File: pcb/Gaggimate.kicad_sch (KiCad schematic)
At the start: 71 parts, among them J1 USB_C_Receptacle, J2 Conn_01x02, J3 Conn_01x03, J4 Conn_01x04, J5 Conn_01x04, J6 Conn_01x10, J7 Conn_01x02, K1 Relay_SPDT, K2 Relay_SPDT, K3 Relay_SPDT, Q1 MMBT3904, Q2 MMBT3904, Q3 MMBT3904, SW1 SW_Push, SW2 SW_Push, U1 ESP32-S3-WROOM-1, U2 AMS1117-3.3, U3 LTV-817S, U4 LTV-817S, U5 LTV-817S, U6 MAX31855EASA

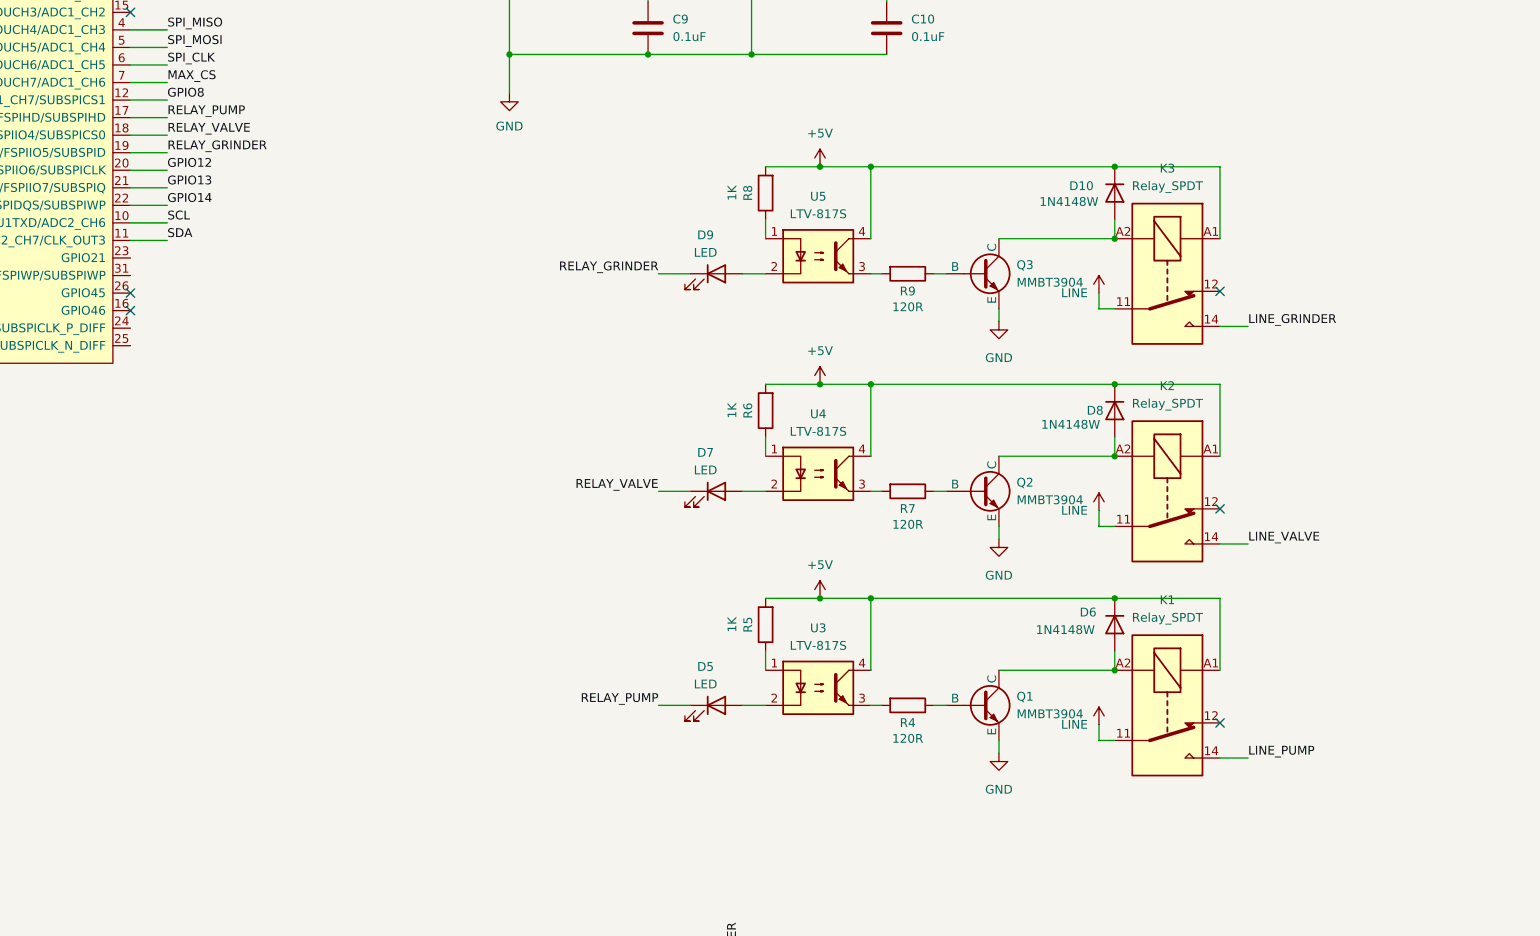
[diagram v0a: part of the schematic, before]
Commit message: feat: Shrink PCB by 16mm
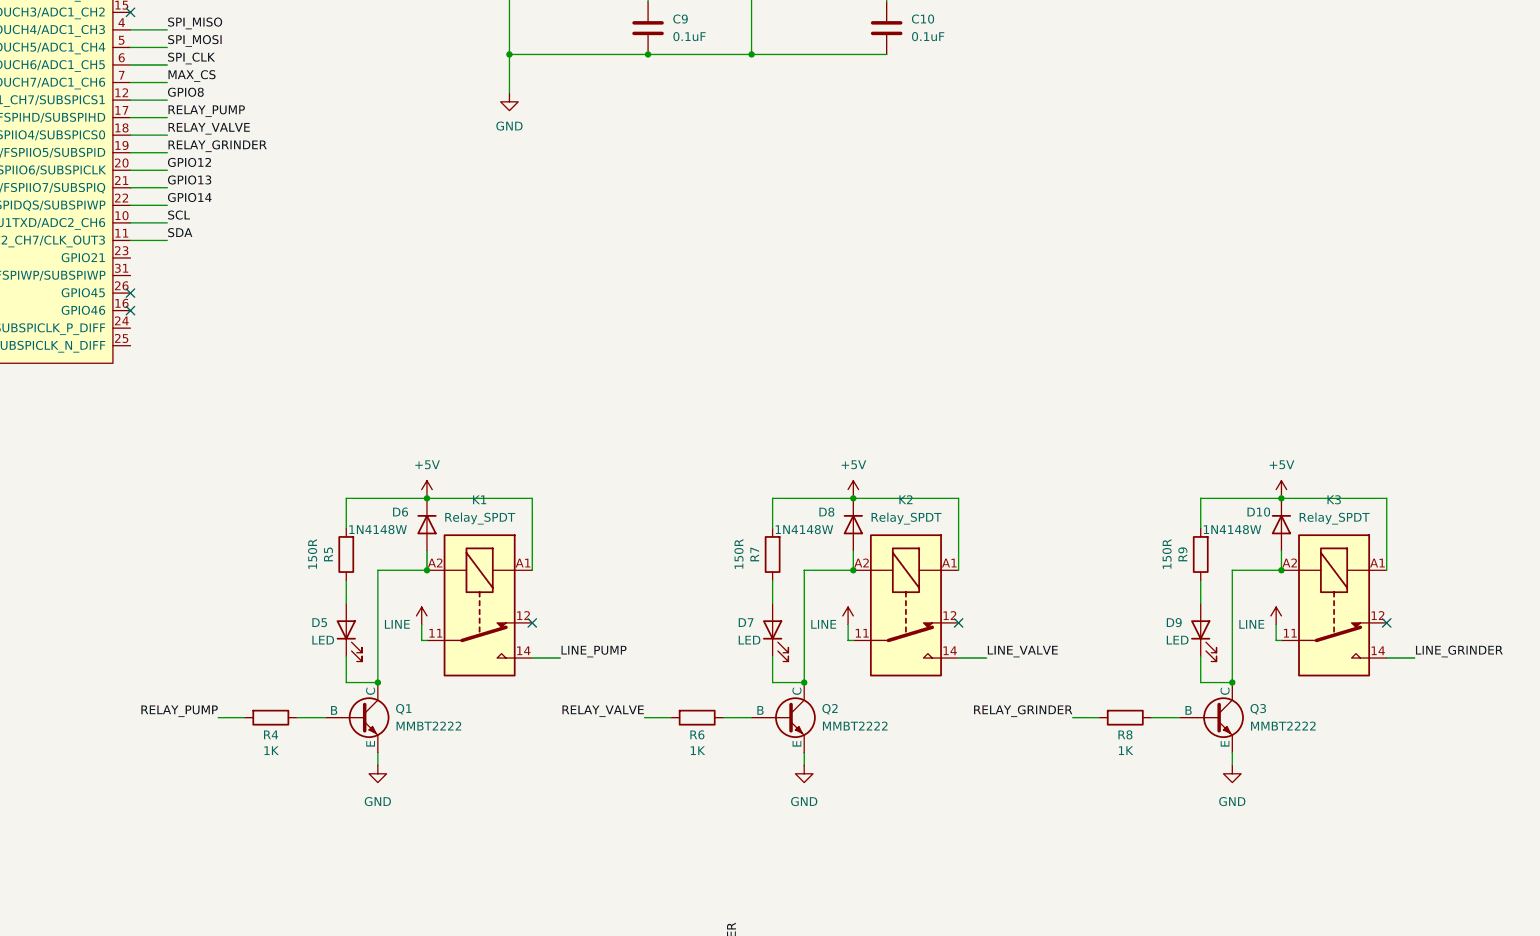
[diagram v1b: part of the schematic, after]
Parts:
- removed U3, U4, U5: LTV-817S, Package_DIP:SMDIP-4_W9.53mm, symbol Isolator:LTV-817S
- Q1, Q2, Q3: value MMBT3904 -> MMBT2222
- R4: value 120R -> 1K
- R5: value 1K -> 150R
- R7, R9: value 120R -> 150R
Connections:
- net +5V: now also R7.2, R9.2; no longer R6.2, R8.2
- net RELAY_GRINDER: now also R8.2; no longer D9.1 (K)
- net RELAY_PUMP: now also R4.2; no longer D5.1 (K)
- net RELAY_VALVE: now also R6.2; no longer D7.1 (K)
- net at D5.2 (A): now also R5.1
- net at D10.2 (A), K3.A2, Q3.1 (C): now also D9.1 (K)
- net at R9.1: now also D9.2 (A); no longer Q3.2 (B)
- net at R8.1: now also Q3.2 (B)
- net at D6.2 (A), K1.A2, Q1.1 (C): now also D5.1 (K)
- net at D8.2 (A), K2.A2, Q2.1 (C): now also D7.1 (K)
- net at R7.1: now also D7.2 (A); no longer Q2.2 (B)
- net at R6.1: now also Q2.2 (B)
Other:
- moved on the sheet: D5, D6, K1, Q1, R4, R5

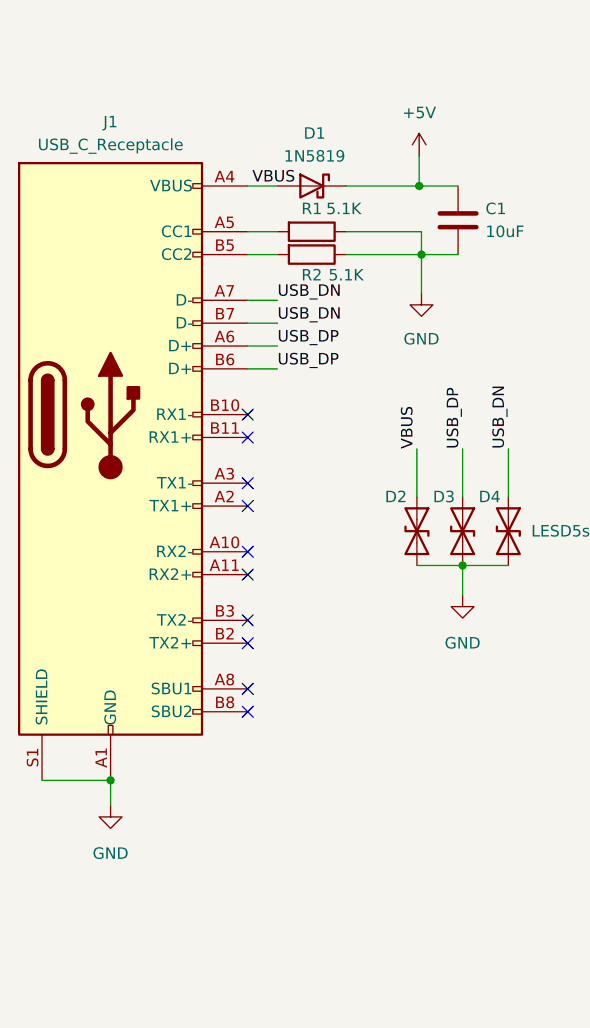
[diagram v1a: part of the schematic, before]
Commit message: feat: Change USB routing on PCB
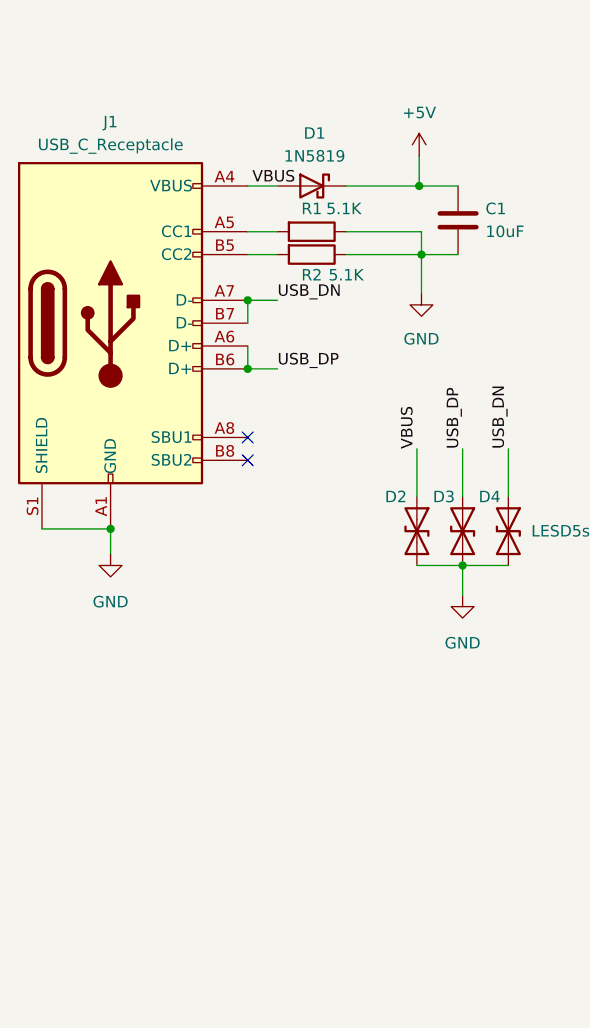
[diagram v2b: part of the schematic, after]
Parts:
- J1: symbol Connector:USB_C_Receptacle -> Connector:USB_C_Receptacle_USB2.0
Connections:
- no-connect marks 16 -> 8
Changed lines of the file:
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@@
   (junction (at 241.046 146.05) (diameter 0) (color 0 0 0 0)
   )
+  (junction (at 40.894 164.592) (diameter 0) (color 0 0 0 0)
+  )
   (junction (at 157.226 152.654) (diameter 0) (color 0 0 0 0)
   )
@@
   (junction (at 361.95 37.084) (diameter 0) (color 0 0 0 0)
   )
+  (junction (at 56.134 146.812) (diameter 0) (color 0 0 0 0)
+  )
   (junction (at 75.438 134.112) (diameter 0) (color 0 0 0 0)
   )
@@
   (junction (at 138.938 152.654) (diameter 0) (color 0 0 0 0)
   )
+  (junction (at 56.134 139.192) (diameter 0) (color 0 0 0 0)
+  )
   (junction (at 148.082 152.654) (diameter 0) (color 0 0 0 0)
   )
@@
   (junction (at 75.184 126.492) (diameter 0) (color 0 0 0 0)
   )
-  (junction (at 40.894 192.532) (diameter 0) (color 0 0 0 0)
-  )
   (junction (at 93.218 42.418) (diameter 0) (color 0 0 0 0)
   )
   (junction (at 127.254 240.792) (diameter 0) (color 0 0 0 0)
   )
-  (no_connect (at 56.134 154.432))
   (no_connect (at 198.12 65.278))
   (no_connect (at 379.984 153.67))
-  (no_connect (at 56.134 167.132))
-  (no_connect (at 56.134 151.892))
+  (no_connect (at 56.134 156.972))
   (no_connect (at 256.286 153.67))
-  (no_connect (at 56.134 184.912))
-  (no_connect (at 56.134 182.372))
-  (no_connect (at 56.134 177.292))
-  (no_connect (at 56.134 174.752))
   (no_connect (at 198.12 108.458))
   (no_connect (at 198.12 105.918))
-  (no_connect (at 56.134 159.512))
-  (no_connect (at 56.134 169.672))
+  (no_connect (at 56.134 154.432))
   (no_connect (at 318.008 153.67))
-  (no_connect (at 56.134 162.052))
   (wire (pts (xy 75.184 126.492) (xy 79.502 126.492))
     (stroke (width 0) (type default))
@@
     (stroke (width 0) (type default))
   )
+  (wire (pts (xy 56.134 139.192) (xy 56.134 141.732))
+    (stroke (width 0) (type default))
+  )
   (wire (pts (xy 129.794 233.172) (xy 129.794 234.442))
     (stroke (width 0) (type default))
@@
     (stroke (width 0) (type default))
   )
-  (wire (pts (xy 56.134 144.272) (xy 59.436 144.272))
-    (stroke (width 0) (type default))
-  )
   (wire (pts (xy 150.114 234.442) (xy 152.4 234.442))
     (stroke (width 0) (type default))
@@
     (stroke (width 0) (type default))
   )
-  (wire (pts (xy 40.894 192.532) (xy 40.894 195.326))
+  (wire (pts (xy 40.894 164.592) (xy 40.894 167.386))
     (stroke (width 0) (type default))
   )
@@
     (stroke (width 0) (type default))
   )
+  (wire (pts (xy 56.134 144.272) (xy 56.134 146.812))
+    (stroke (width 0) (type default))
+  )
   (wire (pts (xy 280.924 37.084) (xy 287.528 37.084))
     (stroke (width 0) (type default))
@@
     (stroke (width 0) (type default))
   )
-  (wire (pts (xy 56.134 141.732) (xy 59.436 141.732))
-    (stroke (width 0) (type default))
-  )
   (wire (pts (xy 308.102 210.058) (xy 308.102 212.344))
     (stroke (width 0) (type default))
@@
     (stroke (width 0) (type default))
   )
-  (wire (pts (xy 33.274 192.532) (xy 40.894 192.532))
+  (wire (pts (xy 33.274 164.592) (xy 40.894 164.592))
     (stroke (width 0) (type default))
   )
@@
     (effects (font (size 1.27 1.27)) (justify left bottom))
   )
-  (label "USB_DN" (at 59.436 141.732 0) (fields_autoplaced)
-    (effects (font (size 1.27 1.27)) (justify left bottom))
-  )
   (label "GPIO13" (at 357.886 44.704 180) (fields_autoplaced)
     (effects (font (size 1.27 1.27)) (justify right bottom))
@@
   )
   (label "SDA" (at 203.454 98.298 0) (fields_autoplaced)
-    (effects (font (size 1.27 1.27)) (justify left bottom))
-  )
-  (label "USB_DP" (at 59.436 144.272 0) (fields_autoplaced)
     (effects (font (size 1.27 1.27)) (justify left bottom))
   )
@@
     )
   )
-  (symbol (lib_id "Connector:USB_C_Receptacle") (at 40.894 151.892 0) (unit 1)
+  (symbol (lib_id "Connector:USB_C_Receptacle_USB2.0") (at 40.894 141.732 0) (unit 1)
     (in_bom yes) (on_board yes) (dnp no) (fields_autoplaced)
     (property "Reference" "J1" (at 40.894 119.38 0)
@@
       (effects (font (size 1.27 1.27)))
     )
-    (property "Footprint" "Connector_USB:USB_C_Receptacle_HRO_TYPE-C-31-M-12" (at 44.704 151.892 0)
-      (effects (font (size 1.27 1.27)) hide)
-    )
-    (property "Datasheet" "https://www.usb.org/sites/default/files/documents/usb_type-c.zip" (at 44.704 151.892 0)
+    (property "Footprint" "Connector_USB:USB_C_Receptacle_HRO_TYPE-C-31-M-12" (at 44.704 141.732 0)
+      (effects (font (size 1.27 1.27)) hide)
+    )
+    (property "Datasheet" "https://www.usb.org/sites/default/files/documents/usb_type-c.zip" (at 44.704 141.732 0)
       (effects (font (size 1.27 1.27)) hide)
     )
     (pin "A1")
-    (pin "A10")
-    (pin "A11")
     (pin "A12")
-    (pin "A2")
-    (pin "A3")
     (pin "A4")
     (pin "A5")
@@
     (pin "A9")
     (pin "B1")
-    (pin "B10")
-    (pin "B11")
     (pin "B12")
-    (pin "B2")
-    (pin "B3")
     (pin "B4")
     (pin "B5")
@@
     )
   )
-  (symbol (lib_id "power:GND") (at 40.894 195.326 0) (unit 1)
-    (in_bom yes) (on_board yes) (dnp no) (fields_autoplaced)
-    (property "Reference" "#PWR03" (at 40.894 201.676 0)
-      (effects (font (size 1.27 1.27)) hide)
-    )
-    (property "Value" "GND" (at 40.894 200.66 0)
-      (effects (font (size 1.27 1.27)))
-    )
-    (property "Footprint" "" (at 40.894 195.326 0)
-      (effects (font (size 1.27 1.27)) hide)
-    )
-    (property "Datasheet" "" (at 40.894 195.326 0)
-      (effects (font (size 1.27 1.27)) hide)
-    )
+  (symbol (lib_id "power:GND") (at 40.894 167.386 0) (unit 1)
+    (in_bom yes) (on_board yes) (dnp no) (fields_autoplaced)
+    (property "Reference" "#PWR03" (at 40.894 173.736 0)
+      (effects (font (size 1.27 1.27)) hide)
+    )
+    (property "Value" "GND" (at 40.894 172.72 0)
+      (effects (font (size 1.27 1.27)))
+    )
+    (property "Footprint" "" (at 40.894 167.386 0)
+      (effects (font (size 1.27 1.27)) hide)
+    )
+    (property "Datasheet" "" (at 40.894 167.386 0)
+      (effects (font (size 1.27 1.27)) hide)
+    )

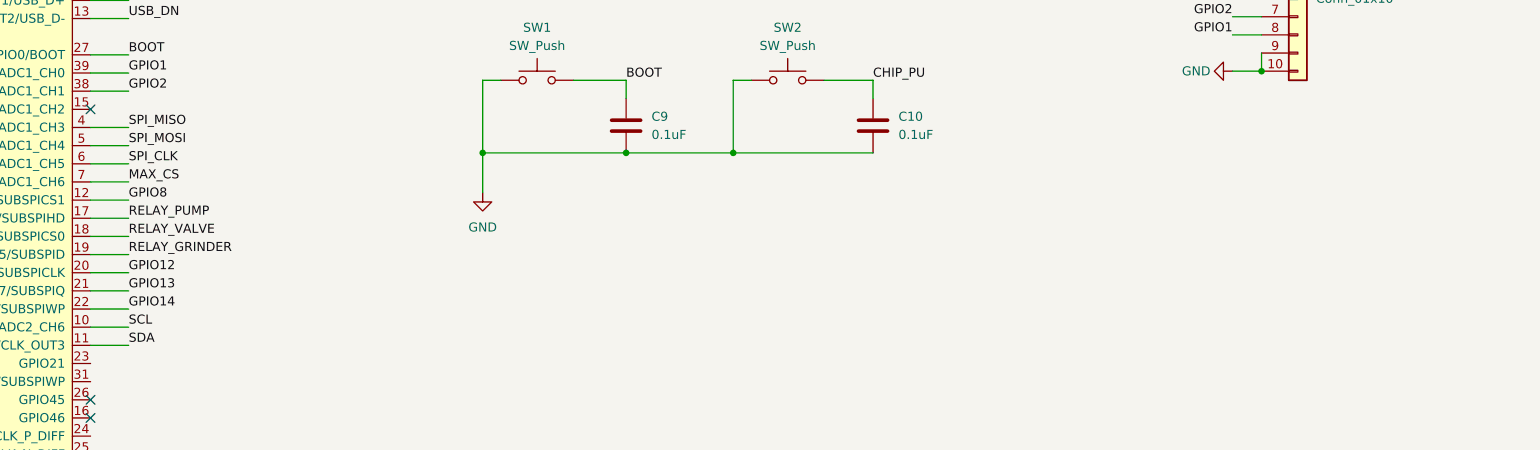
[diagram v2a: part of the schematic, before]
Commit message: fix: Fix PCB buttons, traces
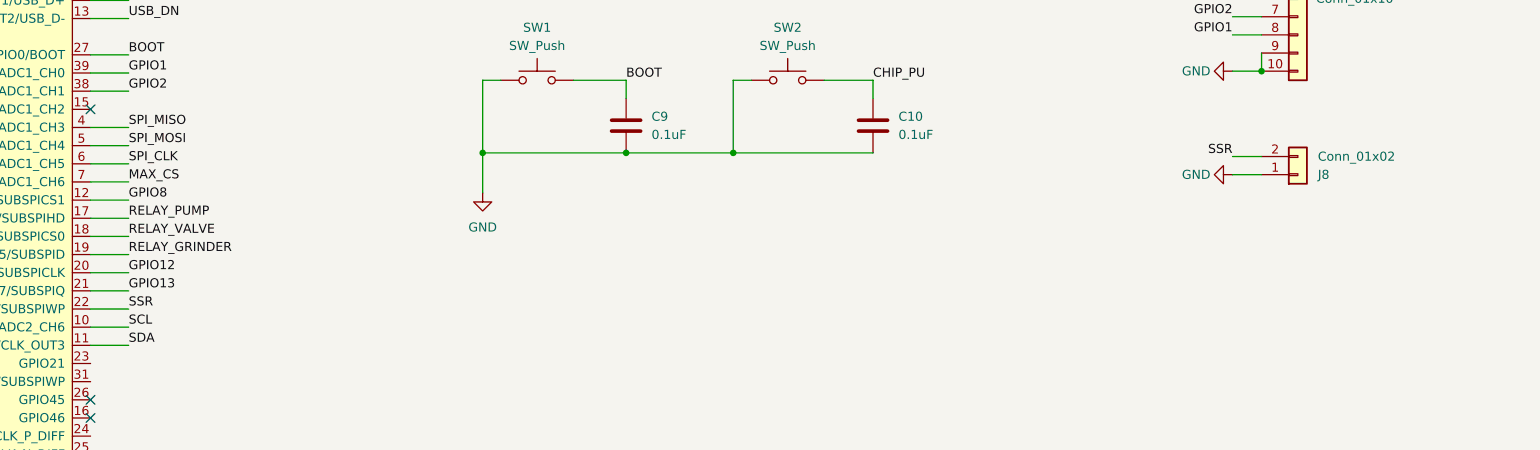
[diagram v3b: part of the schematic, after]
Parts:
- added J8: Conn_01x02, Connector_JST:JST_XH_B2B-XH-A_1x02_P2.50mm_Vertical, symbol Connector_Generic:Conn_01x02
- C1, C2, C4, C6: LCSC (none) -> C15850
- C10, C15, C16, C3, C5, C7, C9: LCSC (none) -> C49678
- C11, C13, C8: LCSC (none) -> C28323
- C14: LCSC (none) -> C1710
- D1: LCSC (none) -> C2891704
- D10, D6, D8: LCSC (none) -> C81598
- D11, D12, D5, D7, D9: LCSC (none) -> C84256
- D2, D3, D4: LCSC (none) -> C383211
- J1: LCSC (none) -> C165948
- J2: LCSC (none) -> C2683165
- J3: LCSC (none) -> C2683166
- J7: LCSC (none) -> C5481312
- K1, K2, K3: LCSC (none) -> C35449
- L1, L2: footprint Inductor_SMD:L_0805_2012Metric -> Inductor_SMD:L_0603_1608Metric; LCSC (none) -> C413961
- PS1: LCSC (none) -> C403745
- Q1, Q2, Q3: LCSC (none) -> C8512
- R1, R2: LCSC (none) -> C27834
- R10, R11, R12, R13, R14, R15, R3: LCSC (none) -> C17414
- R16, R17: LCSC (none) -> C17514
- R18: LCSC (none) -> C17802
- R19, R5, R7, R9: LCSC (none) -> C17471
- R4, R6, R8: LCSC (none) -> C17513
- SW1, SW2: footprint Button_Switch_SMD:SW_SPST_PTS810 -> Button_Switch_SMD:SW_SPST_SKQG_WithStem; LCSC (none) -> C221896
- U1: LCSC (none) -> C2913201
- U2: LCSC (none) -> C6186
- U6: LCSC (none) -> C52028
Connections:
- net GND: now also J8.1 (Pin_1)
- net GPIO14 renamed SSR
- net SSR: now also J8.2 (Pin_2)
